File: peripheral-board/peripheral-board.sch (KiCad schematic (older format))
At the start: 20 parts, among them P1001 Peripheral Bus, P1002 Power, SW1001 Power, U1001 ATTINY48-A, U1002 L78L33ACUTR

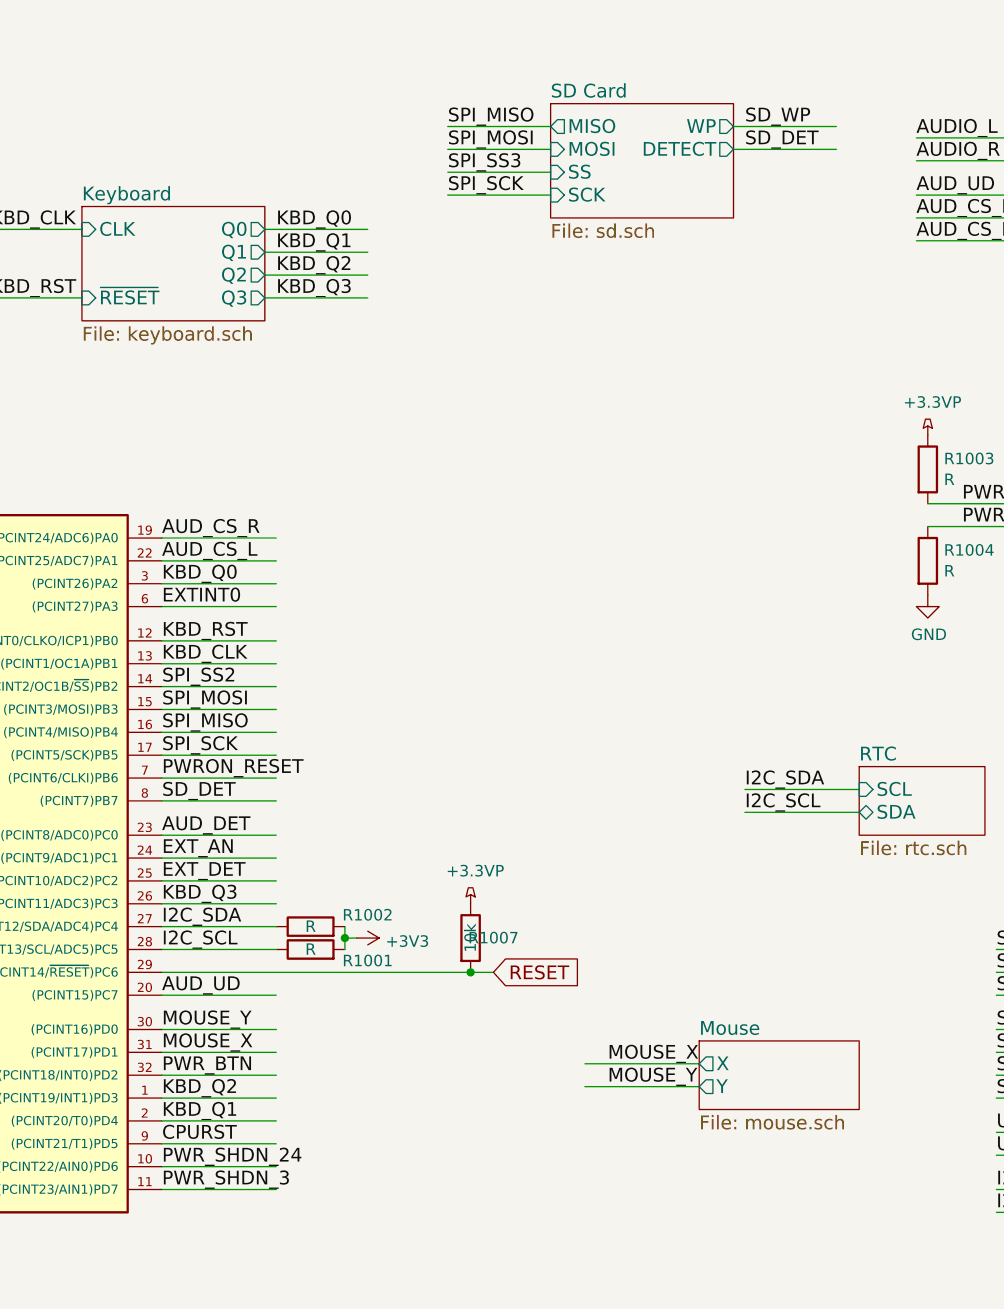
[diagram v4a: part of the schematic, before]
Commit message: fixed various drc errors
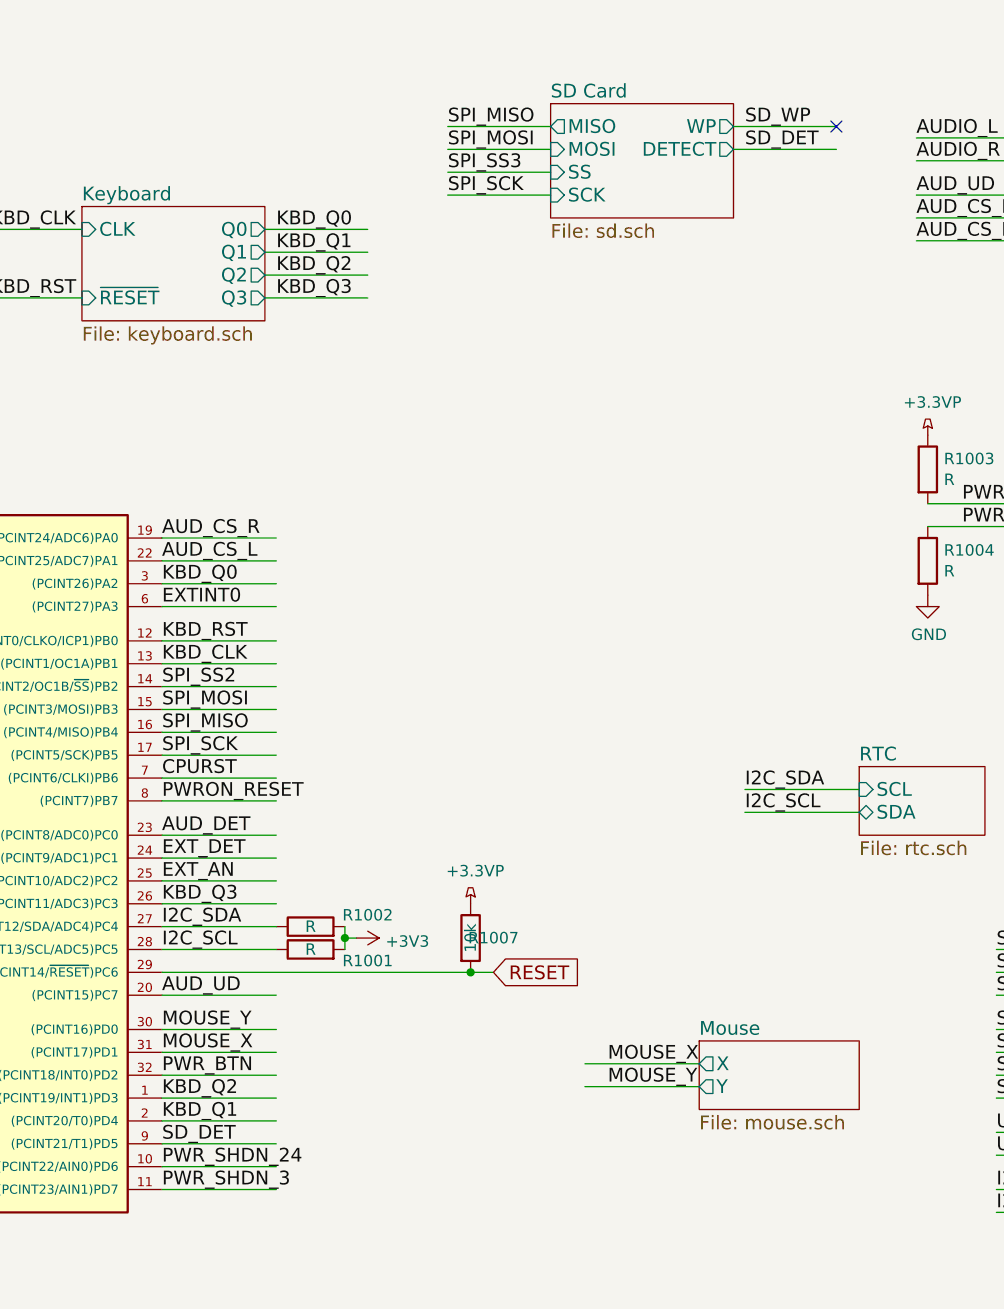
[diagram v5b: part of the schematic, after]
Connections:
- no-connect marks 2 -> 3
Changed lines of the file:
@@
 Text Label 4950 2800 0    60   ~ 0
 AUD_CS_R
+Text Label 4950 4200 0    60   ~ 0
+EXT_DET
 Text Label 4950 4300 0    60   ~ 0
-EXT_DET
-Text Label 4950 4200 0    60   ~ 0
 EXT_AN
 Wire Wire Line
@@
 Wire Wire Line
 	4950 5550 5450 5550
+Text Label 4950 3950 0    60   ~ 0
+PWRON_RESET
 Text Label 4950 3850 0    60   ~ 0
-PWRON_RESET
-Text Label 4950 5450 0    60   ~ 0
 CPURST
 Wire Wire Line
+	4950 3950 5450 3950
+Wire Wire Line
 	4950 3850 5450 3850
-Wire Wire Line
-	4950 5450 5450 5450
 NoConn ~ 1400 1800
 NoConn ~ 1400 2100
@@
 Text Label 7500 1100 0    60   ~ 0
 SD_DET
-Text Label 4950 3950 0    60   ~ 0
+Text Label 4950 5450 0    60   ~ 0
 SD_DET
 Wire Wire Line
@@
 	4950 4400 5450 4400
 Wire Wire Line
-	4950 3950 5450 3950
+	4950 5450 5450 5450
 $Comp
 L LED D1001
@@
 	0    1    1    0
 $EndComp
+NoConn ~ 7900 1000
 $EndSCHEMATC

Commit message: minor fixes
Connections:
- no-connect marks 3 -> 5
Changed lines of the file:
@@
 $EndComp
 NoConn ~ 7900 1000
+NoConn ~ 1400 3800
+NoConn ~ 1400 3900
 $EndSCHEMATC

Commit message: peripheral board all done o____O
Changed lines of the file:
@@
 $Descr A4 11693 8268
 encoding utf-8
-Sheet 1 10
+Sheet 1 8
 Title ""
 Date ""
@@
 F15 "AN" O R 10350 5750 60
 $EndSheet
-$Sheet
-S 10050 850  950  800
-U 581F8966
-F0 "VGA" 60
-F1 "vga.sch" 60
-$EndSheet
-$Comp
+$Comp

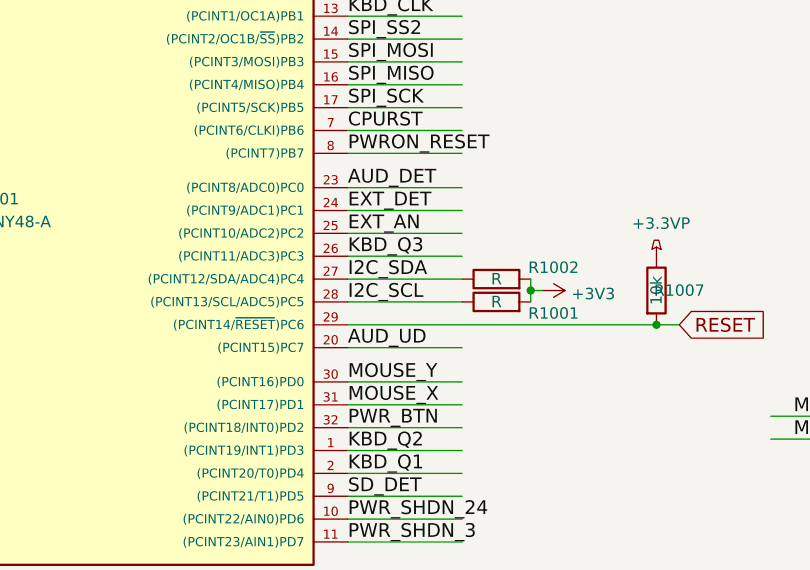
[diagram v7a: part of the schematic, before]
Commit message: mouse connected to adc pins
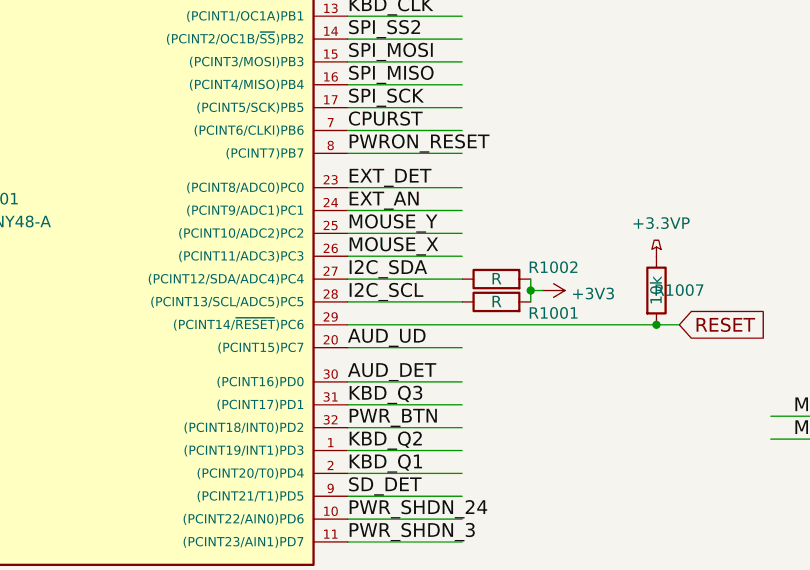
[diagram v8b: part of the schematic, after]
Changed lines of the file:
@@
 Text Label 4950 4600 0    60   ~ 0
 I2C_SCL
-Text Label 4950 5050 0    60   ~ 0
+Text Label 4950 4400 0    60   ~ 0
 MOUSE_X
-Text Label 4950 4950 0    60   ~ 0
+Text Label 4950 4300 0    60   ~ 0
 MOUSE_Y
 $Sheet
@@
 	4950 4600 5450 4600
 Wire Wire Line
-	4950 4950 5450 4950
-Wire Wire Line
-	4950 5050 5450 5050
+	4950 4300 5450 4300
+Wire Wire Line
+	4950 4400 5450 4400
 Wire Wire Line
 	3050 5550 3000 5550
@@
 Text Label 4950 2800 0    60   ~ 0
 AUD_CS_R
+Text Label 4950 4100 0    60   ~ 0
+EXT_DET
 Text Label 4950 4200 0    60   ~ 0
-EXT_DET
-Text Label 4950 4300 0    60   ~ 0
 EXT_AN
 Wire Wire Line
-	5450 4300 4950 4300
+	5450 4200 4950 4200
 Wire Wire Line
 	5450 5150 4950 5150
@@
 Text Label 4950 5250 0    60   ~ 0
 KBD_Q2
-Text Label 4950 4400 0    60   ~ 0
+Text Label 4950 5050 0    60   ~ 0
 KBD_Q3
 Text Label 4950 3350 0    60   ~ 0
@@
 Text Label 9450 1050 0    60   ~ 0
 AUD_DET
-Text Label 4950 4100 0    60   ~ 0
+Text Label 4950 4950 0    60   ~ 0
 AUD_DET
 Wire Wire Line
@@
 SD_DET
 Wire Wire Line
+	4950 4950 5450 4950
+Wire Wire Line
+	4950 4700 6400 4700
+Wire Wire Line
 	4950 4100 5450 4100
 Wire Wire Line
-	4950 4700 6400 4700
-Wire Wire Line
-	4950 4200 5450 4200
-Wire Wire Line
 	4950 4800 5450 4800
 Wire Wire Line
@@
 	4950 5250 5450 5250
 Wire Wire Line
-	4950 4400 5450 4400
+	4950 5050 5450 5050
 Wire Wire Line
 	4950 5450 5450 5450
